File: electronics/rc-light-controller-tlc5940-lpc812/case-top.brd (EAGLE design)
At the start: 26.7 x 18 mm, 0 parts

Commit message: Update documentation and tweak silkscreen
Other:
- board text added: "+"
- board text added: "-"
- board text removed: "GND"
- board text removed: "Vdd"
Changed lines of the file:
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@@
 <wire x1="0" y1="17.034" x2="0" y2="1" width="0" layer="20"/>
 <wire x1="0" y1="1" x2="1" y2="0" width="0" layer="20" curve="90"/>
-<text x="1.27" y="2.54" size="1.016" layer="27" font="vector" ratio="15" align="center-left">GND</text>
-<text x="1.27" y="5.08" size="1.016" layer="27" font="vector" ratio="15" align="center-left">Vdd</text>
+<text x="1.27" y="2.54" size="1.6764" layer="27" font="vector" ratio="15" align="center-left">-</text>
+<text x="1.27" y="5.08" size="1.778" layer="27" font="vector" ratio="15" align="center-left">+</text>
 <text x="1.27" y="7.62" size="1.016" layer="27" font="vector" ratio="15" align="center-left">ST/Rx</text>
 <text x="1.27" y="10.16" size="1.016" layer="27" font="vector" ratio="15" align="center-left">TH/Tx</text>

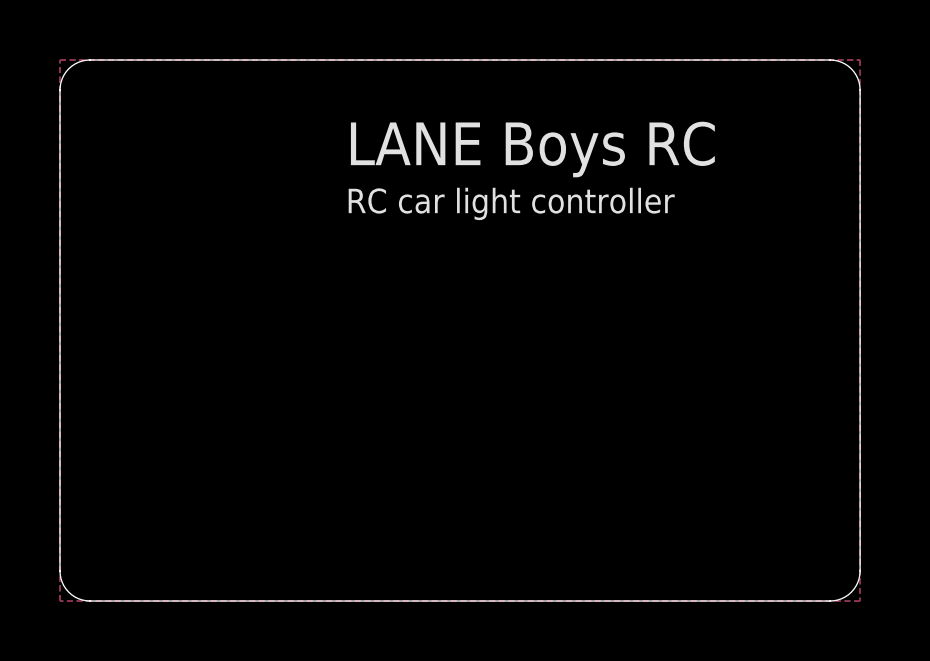
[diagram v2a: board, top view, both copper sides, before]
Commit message: Make board 18x27 mm, not some fraction based on mil
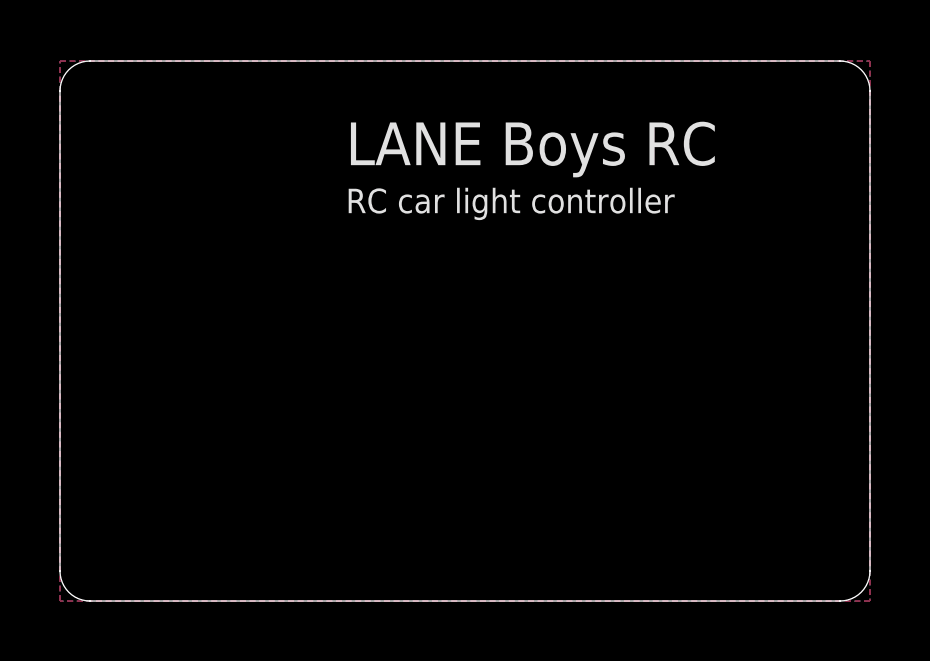
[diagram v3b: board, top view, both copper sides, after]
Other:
- board size 26.7 x 18 mm -> 27 x 18 mm
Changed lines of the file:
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@@
 <setting verticaltext="up"/>
 </settings>
-<grid distance="20" unitdist="mil" unit="mil" style="lines" multiple="1" display="yes" altdistance="0.025" altunitdist="inch" altunit="inch"/>
+<grid distance="39.3700787" unitdist="mil" unit="mil" style="lines" multiple="1" display="yes" altdistance="0.025" altunitdist="inch" altunit="inch"/>
 <layers>
 <layer number="1" name="Top" color="4" fill="1" visible="yes" active="yes"/>
@@
 <board>
 <plain>
-<wire x1="1" y1="0" x2="25.67" y2="0" width="0" layer="20"/>
-<wire x1="25.67" y1="0" x2="26.67" y2="1" width="0" layer="20" curve="90"/>
-<wire x1="26.67" y1="1" x2="26.67" y2="17.034" width="0" layer="20"/>
-<wire x1="26.67" y1="17.034" x2="25.67" y2="18.034" width="0" layer="20" curve="90"/>
-<wire x1="25.67" y1="18.034" x2="1" y2="18.034" width="0" layer="20"/>
-<wire x1="1" y1="18.034" x2="0" y2="17.034" width="0" layer="20" curve="90"/>
-<wire x1="0" y1="17.034" x2="0" y2="1" width="0" layer="20"/>
+<wire x1="1" y1="0" x2="26" y2="0" width="0" layer="20"/>
+<wire x1="26" y1="0" x2="27" y2="1" width="0" layer="20" curve="90"/>
+<wire x1="27" y1="1" x2="27" y2="17" width="0" layer="20"/>
+<wire x1="27" y1="17" x2="26" y2="18" width="0" layer="20" curve="90"/>
+<wire x1="26" y1="18" x2="1" y2="18" width="0" layer="20"/>
+<wire x1="1" y1="18" x2="0" y2="17" width="0" layer="20" curve="90"/>
+<wire x1="0" y1="17" x2="0" y2="1" width="0" layer="20"/>
 <wire x1="0" y1="1" x2="1" y2="0" width="0" layer="20" curve="90"/>
 <text x="1.27" y="2.54" size="1.6764" layer="27" font="vector" ratio="15" align="center-left">-</text>
@@
 <signal name="S$1">
 <polygon width="0.3048" layer="1" isolate="0.3048">
-<vertex x="0" y="18.034"/>
-<vertex x="26.67" y="18.034"/>
-<vertex x="26.67" y="0"/>
+<vertex x="0" y="18"/>
+<vertex x="27" y="18"/>
+<vertex x="27" y="0"/>
 <vertex x="0" y="0"/>
 </polygon>
 <polygon width="0.3048" layer="16" isolate="0.3048">
-<vertex x="0" y="18.034"/>
-<vertex x="26.67" y="18.034"/>
-<vertex x="26.67" y="0"/>
+<vertex x="0" y="18"/>
+<vertex x="27" y="18"/>
+<vertex x="27" y="0"/>
 <vertex x="0" y="0"/>
 </polygon>
